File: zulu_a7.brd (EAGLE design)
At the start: 61 x 25.4 mm, 169 parts, among them J1 Pmod 2x6, Q1 12MHz 25ppm (FPGA + FT2232HQ), Q3 MBT3904DW1T1, U1 XC7A35T-1CPG236C, U10 93LC46BT-I/SN, U2 FT2232HQ USB-UART/JTAG Bridge, U3 AS4C32M16SB-6TIN, U4 W25Q128JVSIQ, U8 LTC3569EUDC#TRPBF, X1 Molex 105017-0001 Micro-USB-B

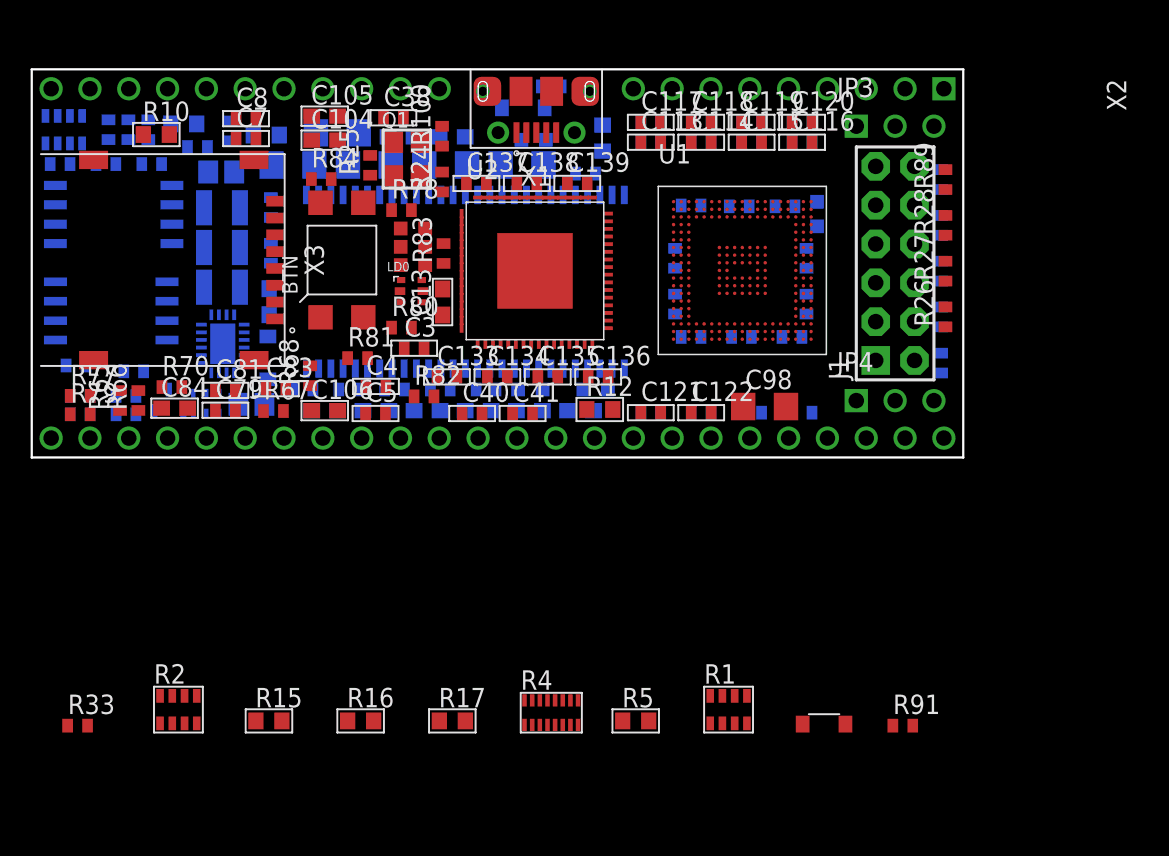
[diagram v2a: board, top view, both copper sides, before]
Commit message: Seat R33 and R91 by hand; D3 has nowhere worth going
R91 lands 8.4 mm from U2's ADBUS2, which is beside the pin it pulls up and as
good as it needs to be. R33 lands 15 mm from U1 ball 1 and 24 from J1 pin 10 --
it is the series resistor between those two, so it wants to be at one END and
is in the middle instead. Usable, not good.

D3 IS STILL PARKED, ON PURPOSE. I said earlier it had a sensible home; that was
wrong, and the error was in what I measured. I checked it fitted within 24 mm of
U1 and reported that as fitting where it belongs. D3 does not belong near U1 --
it belongs at X2 pad 1, because that is where VEXT enters the board. The nearest
free keepout-sized slot to that pin is x 2.60, which is 55.1 mm away at the far
end. A TVS 55 mm downstream of the pin it protects clamps almost nothing; the
inductance in between is the whole problem the part exists to solve. Placing it
there makes the board look finished and the part do nothing, so it stays parked,
where it is visibly unplaced. The corner it wants is JP3's band plus X2's pad
keepout, and dropping JP3/JP4 frees exactly that corner.

A first attempt put D3 at x 16.15 and the generator rejected it outright:
X3's layer-39 card-eject stroke reaches well past its body, and my own free-space
map had been counting copper and silk but not keepouts. The check caught what
the map missed, which is the arrangement working as intended.

D2 is pinned at 30.32, 19.79 on the back, where the anchored pass had already
put it. Seating two parts by hand changed what was free, the pass re-ran, and D2
fell out -- on a board this full every hand placement pushes something else off.
Pinning it stops the shuffle costing more than it buys.

Real parts parked: 10 -> 8. check_board 0 findings.

Co-Authored-By: Claude Opus 5 <noreply@anthropic.com>
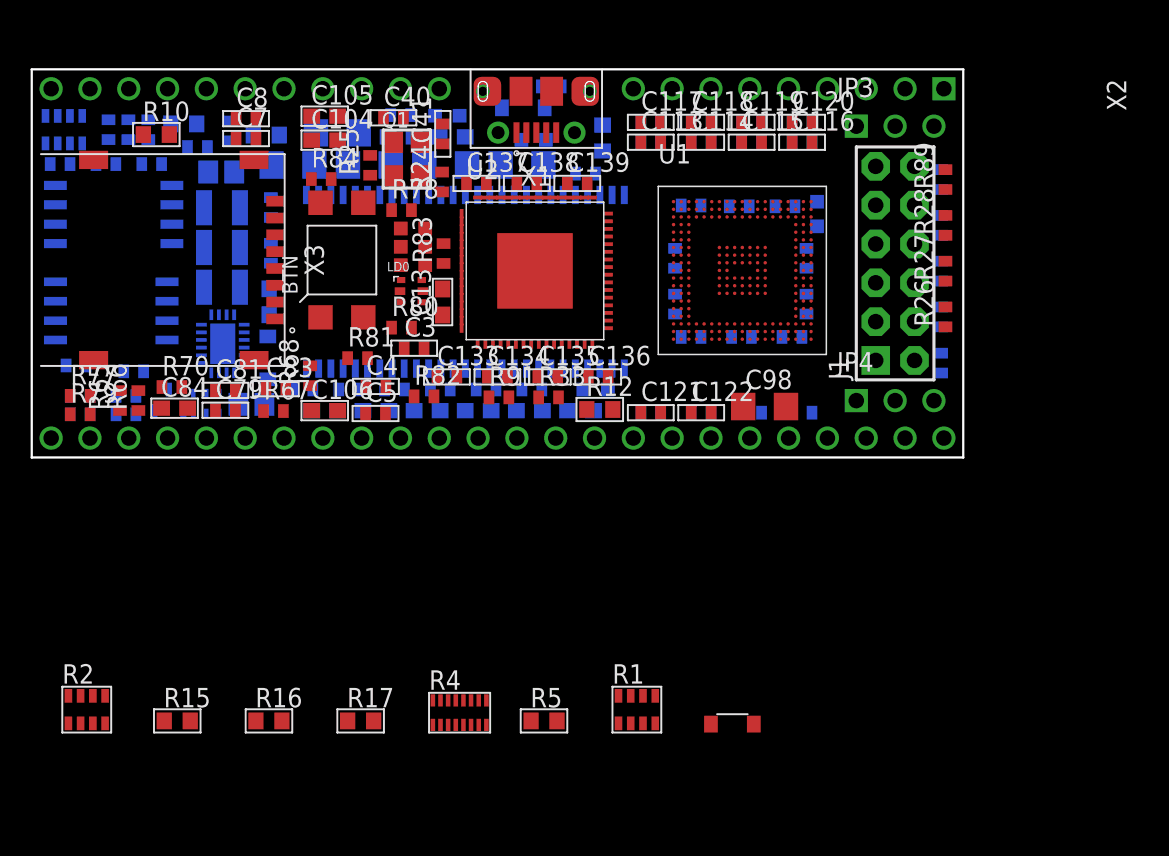
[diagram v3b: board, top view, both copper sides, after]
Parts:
- moved R33 37.6 mm to (33.8, 3.93)
- moved R91 34.1 mm to (30.6, 3.93)
- moved C40 20.0 mm to (23.7, 22.2)
- moved C41 19.0 mm to (26.9, 21.2), turned to 90 degrees
- moved R100 16.9 mm to (23.7, 4.45), flipped to the bottom, turned to 0 degrees
- moved L4 16.3 mm to (32.8, 20.8)
- moved R16 6.00 mm to (15.5, -17.2)
- moved R2 6.00 mm to (2.80, -16.5)
- moved D3 6.00 mm to (45.9, -17.4)
- moved R1 6.00 mm to (38.8, -16.5)
- moved R15 6.00 mm to (9.52, -17.2)
- moved R17 6.00 mm to (21.5, -17.2)
- moved R4 6.00 mm to (28.0, -16.7)
- moved R5 6.00 mm to (33.5, -17.2)
- moved L5 5.86 mm to (27.2, 22.4)
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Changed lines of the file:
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@@
 </autorouter>
 <elements>
-<element name="R100" library="rcl" package="R0402" value="330" x="26.85" y="21.024" rot="R90"/>
+<element name="R100" library="rcl" package="R0402" value="330" x="23.74" y="4.45" rot="MR0"/>
 <element name="R101" library="rcl" package="R0402" value="2.21k" x="1.858" y="19.2" rot="MR0"/>
 <element name="R96" library="rcl" package="R0402" value="10k" x="4.854" y="19.2" rot="MR0"/>
 <element name="R97" library="rcl" package="R0402" value="10k" x="7.85" y="19.2" rot="MR0"/>
 <element name="R98" library="rcl" package="R0402" value="10k" x="10.846" y="20.318" rot="MR0"/>
-<element name="R99" library="rcl" package="R0402" value="4.7k" x="23.74" y="4.45" rot="MR0"/>
+<element name="R99" library="rcl" package="R0402" value="4.7k" x="26.736" y="4.45" rot="MR0"/>
 <element name="C133" library="rcl" package="C0402" value="0.1uF" x="27.1705" y="5.2705"/>
 <element name="C134" library="rcl" package="C0402" value="0.1uF" x="30.4705" y="5.2705"/>
@@
 <element name="R31" library="rcl" package="R0402" value="200" x="59.5098" y="15.19" rot="MR90"/>
 <element name="R32" library="rcl" package="R0402" value="200" x="33.998" y="24.284" rot="MR0"/>
-<element name="R33" library="rcl" package="R0402" value="200" x="3" y="-17.55"/>
+<element name="R33" library="rcl" package="R0402" value="200" x="33.823" y="3.933"/>
 <element name="U$2" library="ctambe" package="CC_CC" value="" x="5.0585" y="-6.4415"/>
 <element name="U$3" library="ctambe" package="CC_BY" value="" x="10.895" y="-7.722"/>
@@
 <element name="R34" library="ctambe" package="742C083" value="4.7K" x="2.9" y="21.45" rot="MR0"/>
 <element name="R35" library="rcl" package="R0402" value="4.7K" x="2.898" y="6.02" rot="MR0"/>
-<element name="R2" library="ctambe" package="742C083" value="4.7K" x="8.8" y="-16.5"/>
+<element name="R2" library="ctambe" package="742C083" value="4.7K" x="2.8" y="-16.5"/>
 <element name="U1" library="ctambe" package="XC7A35T-CPG236" value="XC7A35T-1CPG236C" x="42" y="16.74"/>
 <element name="R10" library="rcl" package="R0603" value="2.32K" x="8.154" y="21.132"/>
@@
 <element name="R13" library="rcl" package="R0603" value="845" x="37.357" y="20.904" rot="MR90"/>
 <element name="R14" library="rcl" package="R0603" value="2.32K" x="9.949" y="21.83" rot="MR0"/>
-<element name="R15" library="rcl" package="R0603" value="1K" x="15.524" y="-17.238"/>
-<element name="R16" library="rcl" package="R0603" value="140" x="21.524" y="-17.238"/>
-<element name="R17" library="rcl" package="R0603" value="845" x="27.524" y="-17.238"/>
+<element name="R15" library="rcl" package="R0603" value="1K" x="9.524" y="-17.238"/>
+<element name="R16" library="rcl" package="R0603" value="140" x="15.524" y="-17.238"/>
+<element name="R17" library="rcl" package="R0603" value="845" x="21.524" y="-17.238"/>
 <element name="C3" library="rcl" package="C0402" value="0.1uF" x="25.025" y="7.15"/>
 <element name="C4" library="rcl" package="C0402" value="0.1uF" x="22.525" y="4.65"/>
@@
 <element name="JP3" library="pinhead" package="1X03-NOSILK" value="JTAG TCK/TMS/GND" x="56.5" y="21.68"/>
 <element name="JP4" library="pinhead" package="1X03-NOSILK" value="JTAG TDI/TDO/3V3" x="56.5" y="3.72"/>
-<element name="R4" library="ctambe" package="741X163" value="100" x="34" y="-16.7"/>
-<element name="R5" library="rcl" package="R0603" value="5.1K" x="39.524" y="-17.238"/>
-<element name="R1" library="ctambe" package="742C083" value="4.7K" x="44.8" y="-16.5"/>
+<element name="R4" library="ctambe" package="741X163" value="100" x="28" y="-16.7"/>
+<element name="R5" library="rcl" package="R0603" value="5.1K" x="33.524" y="-17.238"/>
+<element name="R1" library="ctambe" package="742C083" value="4.7K" x="38.8" y="-16.5"/>
 <element name="U8" library="ctambe" package="LTC3569-QFN20" value="LTC3569EUDC#TRPBF" x="12.5" y="7.44" rot="MR0"/>
 <element name="D1" library="ctambe" package="SOD123" value="PMEG2020EJ,115" x="15.45" y="6.518" rot="MR90"/>
 <element name="D2" library="ctambe" package="SOD123" value="PMEG2020EJ,115" x="32.17" y="22.884" rot="MR0"/>
-<element name="D3" library="ctambe" package="SOD123" value="SMF5.0A" x="51.85" y="-17.45"/>
+<element name="D3" library="ctambe" package="SOD123" value="SMF5.0A" x="45.85" y="-17.45"/>
 <element name="C78" library="rcl" package="C0805" value="22uF 10V" x="12.401" y="18.679" rot="MR0"/>
 <element name="R67" library="rcl" package="R0402" value="3.48K 1%" x="15.821" y="3.04"/>
@@
 <element name="C82" library="rcl" package="C0603" value="10uF" x="15.535" y="10.192" rot="MR90"/>
 <element name="L3" library="ctambe" package="IND2520" value="2.2uH" x="12.45" y="16.34" rot="MR0"/>
-<element name="L4" library="ctambe" package="IND0603" value="FB 600R@100MHz" x="32.63" y="4.45" rot="MR0"/>
-<element name="L5" library="ctambe" package="IND0603" value="FB 600R@100MHz" x="32.845" y="20.79" rot="MR0"/>
+<element name="L4" library="ctambe" package="IND0603" value="FB 600R@100MHz" x="32.845" y="20.79" rot="MR0"/>
+<element name="L5" library="ctambe" package="IND0603" value="FB 600R@100MHz" x="27.196" y="22.36" rot="MR0"/>
 <element name="L6" library="ctambe" package="IND0603" value="FB 600R@100MHz" x="51.392" y="15.932" rot="MR90"/>
 <element name="L7" library="ctambe" package="IND0603" value="FB 600R@100MHz" x="36.9" y="4.45" rot="MR0"/>
 <element name="C123" library="rcl" package="C0402" value="100nF" x="49.75" y="7.89" rot="MR0"/>
 <element name="C124" library="rcl" package="C0402" value="470nF" x="43.15" y="16.49" rot="MR0"/>
-<element name="R18" library="rcl" package="R0402" value="12K 1%" x="26.736" y="4.45" rot="MR0"/>
-<element name="R19" library="rcl" package="R0402" value="10K" x="29.732" y="4.45" rot="MR0"/>
+<element name="R18" library="rcl" package="R0402" value="12K 1%" x="29.732" y="4.45" rot="MR0"/>
+<element name="R19" library="rcl" package="R0402" value="10K" x="32.728" y="4.45" rot="MR0"/>
 <element name="R20" library="rcl" package="R0402" value="1K" x="46.298" y="16.44" rot="MR0"/>
 <element name="R21" library="rcl" package="R0402" value="1K" x="49.294" y="16.44" rot="MR0"/>
@@
 <element name="C139" library="rcl" package="C0402" value="3.3uF" x="35.7" y="17.933"/>
 <element name="C39" library="rcl" package="C0402" value="3.3uF" x="36.234" y="18.58" rot="MR0"/>
-<element name="C40" library="rcl" package="C0402" value="100nF" x="28.821" y="2.878"/>
-<element name="C41" library="rcl" package="C0402" value="100nF" x="32.121" y="2.878"/>
+<element name="C40" library="rcl" package="C0402" value="100nF" x="23.6705" y="22.23"/>
+<element name="C41" library="rcl" package="C0402" value="100nF" x="26.9" y="21.176" rot="R90"/>
 <element name="R71" library="rcl" package="R0402" value="180K 1%" x="6.169" y="2.828" rot="MR0"/>
 <element name="C83" library="rcl" package="C0402" value="20pF" x="15.973" y="4.5"/>
@@
 <element name="R89" library="rcl" package="R0402" value="10K" x="59.79" y="18.186" rot="R90"/>
 <element name="R90" library="rcl" package="R0402" value="10K" x="59.5098" y="6.176" rot="MR90"/>
-<element name="R91" library="rcl" package="R0402" value="10K" x="57" y="-17.55"/>
+<element name="R91" library="rcl" package="R0402" value="10K" x="30.573" y="3.933"/>
 <element name="R92" library="rcl" package="R0402" value="10K" x="59.5098" y="18.186" rot="MR90"/>
 <element name="R93" library="rcl" package="R0402" value="10K" x="42.1" y="13.034" rot="MR90"/>
@@
 <element name="BTN" library="ctambe" package="PTA-142" value="PTA-142" x="20.3" y="12.92" rot="R90"/>
 <element name="Q1" library="ctambe" package="32X25" value="12MHz 25ppm (FPGA + FT2232HQ)" x="23.7" y="20.63"/>
-<element name="C38" library="rcl" package="C0402" value="0.01uF" x="23.6705" y="22.23"/>
+<element name="C38" library="rcl" package="C0402" value="0.01uF" x="24.146" y="22.41" rot="MR0"/>
 <element name="J1" library="ctambe" package="2X06" value="Pmod 2x6" x="56.5" y="12.7" rot="R90"/>
 <element name="R24" library="rcl" package="R0402" value="33" x="26.85" y="18.028" rot="R90"/>
